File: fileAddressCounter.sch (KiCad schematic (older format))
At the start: 16 parts, among them U13 CD74AC161M, U14 CD74AC161M, U16 CD74AC161M, U17 CD74AC161M, U18 74AHC1G04, U19 CD74AC161M, U20 CD74AC161M, U38 74AHC1G04, U39 74AHC1G04

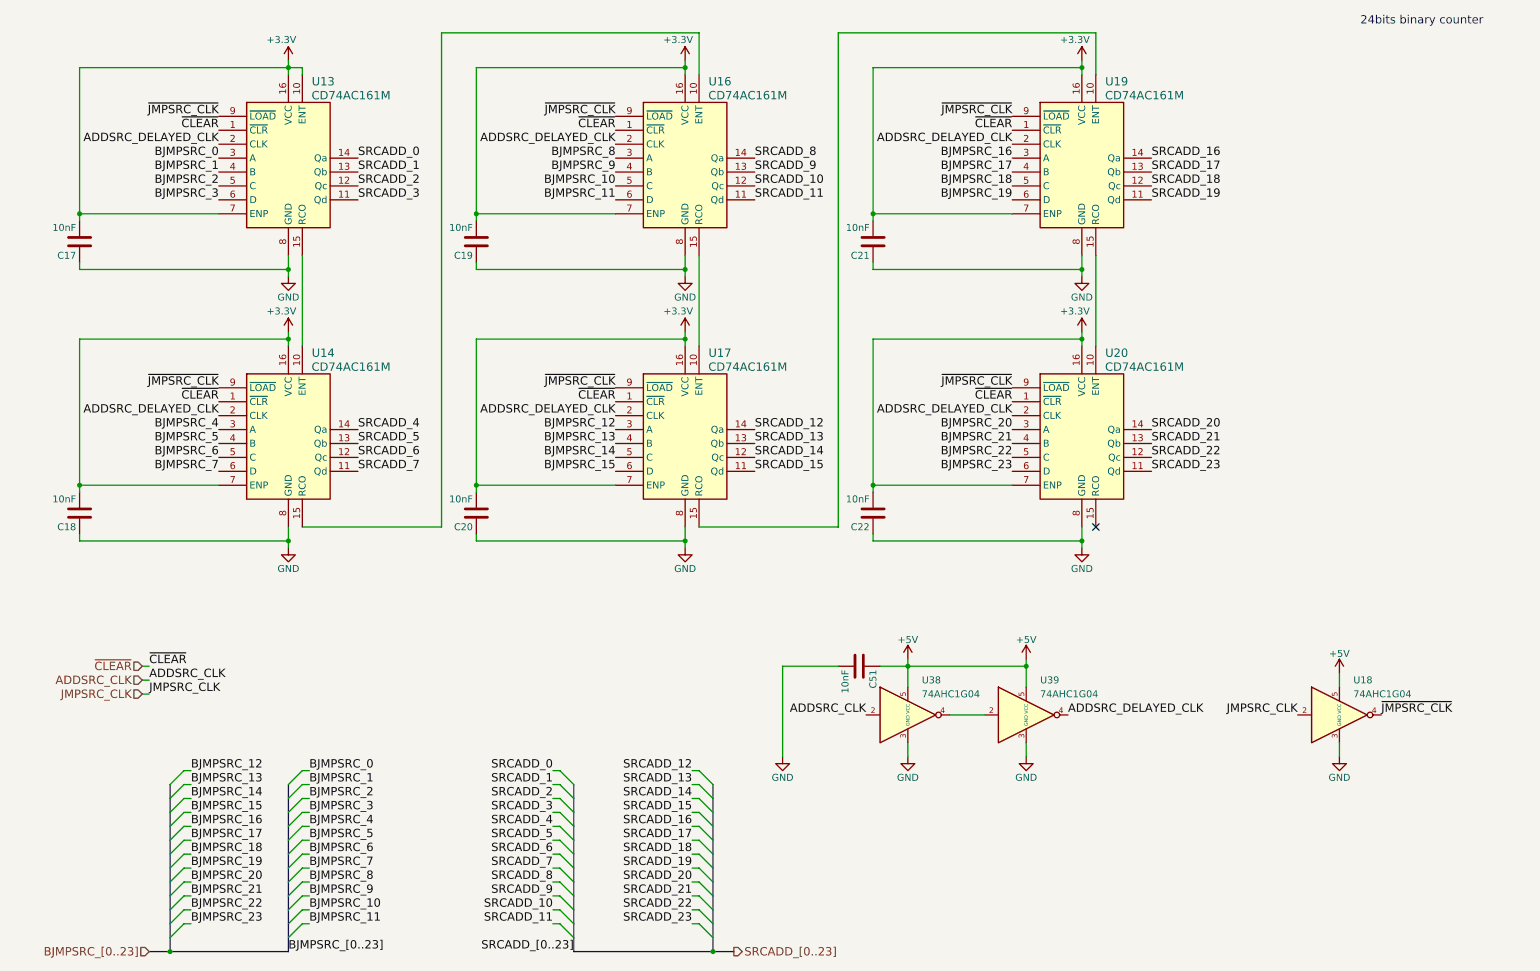
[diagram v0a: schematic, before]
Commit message: V5.1 (#15)
* Remove compatibility for 5.0, 4.x and add 5.1+

* Fix switched pins on SN74LV393A #7

* Removed capacitor on 12V #11

* Add/Modify power decoupling capacitor #10

* Removing ADDSCR_CLK delay #9

* Schematics : set version 5.1, 2021 copyright and publish date

* Put non-electrolytic capacitor #10

* Set every capacitor size to 0805

* Add new footprint for J7 TE_3-641124-6 #6

* Schematic : set pinHeader on J12 #4

* Netlist, apply change to board, clean track, #6 #4 #12 #10

* Set version to 5.1, 2021 copyright and date, replace the missing QRcode

* Back the MM1 connectors #8

* Replace capacitor for U22 U23 U24 #13

* Better decoupling

* Increase version, year to 2021, clear status

* Precise the molex connector for power supply

* First step, import ses

* Clean bottom layer

* #14 Set the BWRITE2 bus instead of BWRITE1 on U12

* netlist, redo autorouting and cleaning

* use shields.io for colored badge

* Update gerbert files

* Changelog, updated BOM

* Small revision on blockDiagram

* Update README.md

* exporting pcb in pdf

* 3D images, diagram.png

* Update schematics pdf

* redo wavedrom_24bitsCounter
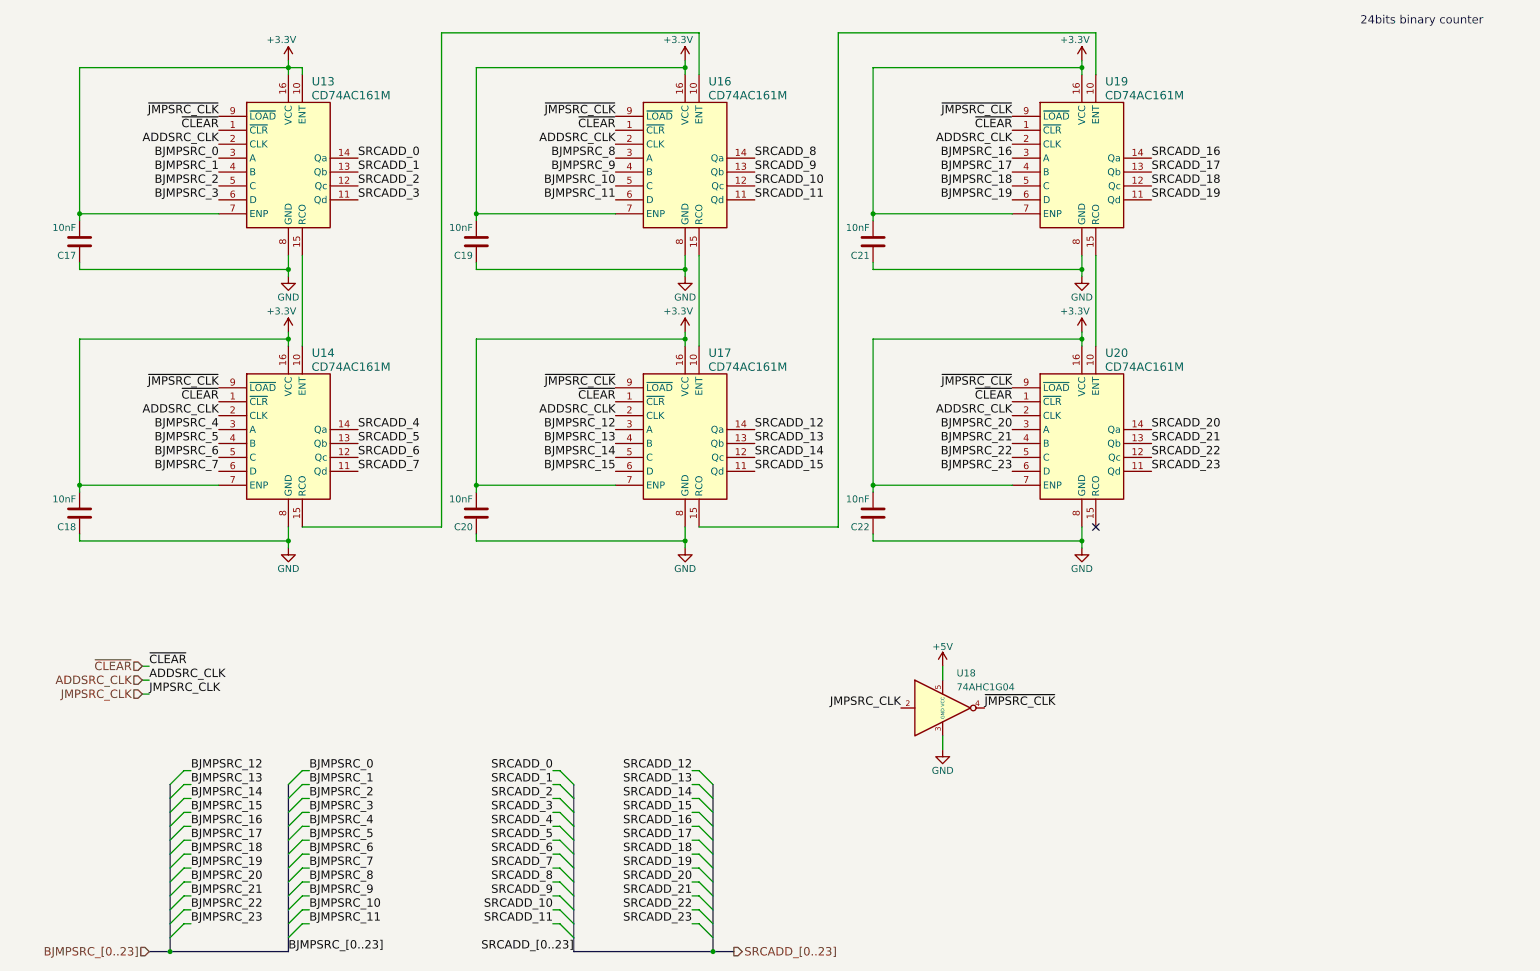
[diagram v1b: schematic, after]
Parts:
- removed C51: 10nF, Capacitor_SMD:C_0805_2012Metric, symbol Device:C
- removed U38, U39: 74AHC1G04, Package_TO_SOT_SMD:SOT-23-5, symbol Custom:74AHC1G04
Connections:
- net ADDSRC_DELAYED_CLK is gone; now on net ADDSRC_CLK: U13.2 (CLK), U14.2 (CLK), U16.2 (CLK), U17.2 (CLK), U19.2 (CLK), U20.2 (CLK)
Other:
- moved on the sheet: U18
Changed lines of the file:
@@
 Sheet 6 10
 Title "GCM"
-Date "2020-11-23"
-Rev "V5.0"
+Date "2021-02-16"
+Rev "V5.1"
 Comp "Guillaume Guillet"
-Comment1 "Copyright Guillaume Guillet 2020"
+Comment1 "Copyright Guillaume Guillet 2021"
 Comment2 "Licensed under CERN-OHL-W v2 or later"
 Comment3 ""
@@
 L power:GND #PWR083
 U 1 1 5BB5F937
-P 9950 5900
+P 7100 5850
 AR Path="/5BB5F937" Ref="#PWR083"  Part="1"
 AR Path="/5A93FC93/5BB5F937" Ref="#PWR083"  Part="1"
-F 0 "#PWR083" H 9950 5650 50  0001 C CNN
-F 1 "GND" H 9950 5750 50  0000 C CNN
-F 2 "" H 9950 5900 50  0001 C CNN
-F 3 "" H 9950 5900 50  0001 C CNN
-	1    9950 5900
+F 0 "#PWR083" H 7100 5600 50  0001 C CNN
+F 1 "GND" H 7100 5700 50  0000 C CNN
+F 2 "" H 7100 5850 50  0001 C CNN
+F 3 "" H 7100 5850 50  0001 C CNN
+	1    7100 5850
 	1    0    0    -1
 $EndComp
@@
 L power:+5V #PWR084
 U 1 1 5BB5F9A2
-P 9950 5300
+P 7100 5250
 AR Path="/5BB5F9A2" Ref="#PWR084"  Part="1"
 AR Path="/5A93FC93/5BB5F9A2" Ref="#PWR084"  Part="1"
-F 0 "#PWR084" H 9950 5150 50  0001 C CNN
-F 1 "+5V" H 9950 5440 50  0000 C CNN
-F 2 "" H 9950 5300 50  0001 C CNN
-F 3 "" H 9950 5300 50  0001 C CNN
-	1    9950 5300
-	1    0    0    -1
-$EndComp
-Text Label 9650 5600 2    60   ~ 0
+F 0 "#PWR084" H 7100 5100 50  0001 C CNN
+F 1 "+5V" H 7100 5390 50  0000 C CNN
+F 2 "" H 7100 5250 50  0001 C CNN
+F 3 "" H 7100 5250 50  0001 C CNN
+	1    7100 5250
+	1    0    0    -1
+$EndComp
+Text Label 6800 5550 2    60   ~ 0
 JMPSRC_CLK
-Text Label 10250 5600 0    60   ~ 0
+Text Label 7400 5550 0    60   ~ 0
 ~JMPSRC_CLK
 Text Label 2550 6000 0    60   ~ 0
@@
 L Custom:74AHC1G04 U?
 U 1 1 5F9095CA
-P 9950 5600
+P 7100 5550
 AR Path="/5F9095CA" Ref="U?"  Part="1"
 AR Path="/5A93FC93/5F9095CA" Ref="U18"  Part="1"
-F 0 "U18" H 10050 5850 50  0000 L CNN
-F 1 "74AHC1G04" H 10050 5750 50  0000 L CNN
-F 2 "Package_TO_SOT_SMD:SOT-23-5" H 9950 5600 50  0001 C CNN
-F 3 "https://assets.nexperia.com/documents/data-sheet/74AHC_AHCT1G04.pdf" H 9950 5600 50  0001 C CNN
-	1    9950 5600
-	1    0    0    -1
-$EndComp
-Wire Wire Line
-	9950 5900 9950 5800
-Wire Wire Line
-	9950 5400 9950 5300
-$Comp
-L power:GND #PWR?
-U 1 1 5FB1C83D
-P 7700 5900
-AR Path="/5FB1C83D" Ref="#PWR?"  Part="1"
-AR Path="/5A93FC93/5FB1C83D" Ref="#PWR0163"  Part="1"
-F 0 "#PWR0163" H 7700 5650 50  0001 C CNN
-F 1 "GND" H 7700 5750 50  0000 C CNN
-F 2 "" H 7700 5900 50  0001 C CNN
-F 3 "" H 7700 5900 50  0001 C CNN
-	1    7700 5900
-	1    0    0    -1
-$EndComp
-$Comp
-L power:+5V #PWR?
-U 1 1 5FB1C843
-P 7700 5200
-AR Path="/5FB1C843" Ref="#PWR?"  Part="1"
-AR Path="/5A93FC93/5FB1C843" Ref="#PWR0164"  Part="1"
-F 0 "#PWR0164" H 7700 5050 50  0001 C CNN
-F 1 "+5V" H 7700 5340 50  0000 C CNN
-F 2 "" H 7700 5200 50  0001 C CNN
-F 3 "" H 7700 5200 50  0001 C CNN
-	1    7700 5200
-	1    0    0    -1
-$EndComp
-$Comp
-L Custom:74AHC1G04 U?
-U 1 1 5FB1C84B
-P 7700 5600
-AR Path="/5FB1C84B" Ref="U?"  Part="1"
-AR Path="/5A93FC93/5FB1C84B" Ref="U39"  Part="1"
-F 0 "U39" H 7800 5850 50  0000 L CNN
-F 1 "74AHC1G04" H 7800 5750 50  0000 L CNN
-F 2 "Package_TO_SOT_SMD:SOT-23-5" H 7700 5600 50  0001 C CNN
-F 3 "https://assets.nexperia.com/documents/data-sheet/74AHC_AHCT1G04.pdf" H 7700 5600 50  0001 C CNN
-	1    7700 5600
-	1    0    0    -1
-$EndComp
-Wire Wire Line
-	7700 5900 7700 5800
-$Comp
-L power:GND #PWR?
-U 1 1 5FB2A8C2
-P 6850 5900
-AR Path="/5FB2A8C2" Ref="#PWR?"  Part="1"
-AR Path="/5A93FC93/5FB2A8C2" Ref="#PWR0165"  Part="1"
-F 0 "#PWR0165" H 6850 5650 50  0001 C CNN
-F 1 "GND" H 6850 5750 50  0000 C CNN
-F 2 "" H 6850 5900 50  0001 C CNN
-F 3 "" H 6850 5900 50  0001 C CNN
-	1    6850 5900
-	1    0    0    -1
-$EndComp
-$Comp
-L power:+5V #PWR?
-U 1 1 5FB2A8C8
-P 6850 5200
-AR Path="/5FB2A8C8" Ref="#PWR?"  Part="1"
-AR Path="/5A93FC93/5FB2A8C8" Ref="#PWR0166"  Part="1"
-F 0 "#PWR0166" H 6850 5050 50  0001 C CNN
-F 1 "+5V" H 6850 5340 50  0000 C CNN
-F 2 "" H 6850 5200 50  0001 C CNN
-F 3 "" H 6850 5200 50  0001 C CNN
-	1    6850 5200
-	1    0    0    -1
-$EndComp
-$Comp
-L Custom:74AHC1G04 U?
-U 1 1 5FB2A8CE
-P 6850 5600
-AR Path="/5FB2A8CE" Ref="U?"  Part="1"
-AR Path="/5A93FC93/5FB2A8CE" Ref="U38"  Part="1"
-F 0 "U38" H 6950 5850 50  0000 L CNN
-F 1 "74AHC1G04" H 6950 5750 50  0000 L CNN
-F 2 "Package_TO_SOT_SMD:SOT-23-5" H 6850 5600 50  0001 C CNN
-F 3 "https://assets.nexperia.com/documents/data-sheet/74AHC_AHCT1G04.pdf" H 6850 5600 50  0001 C CNN
-	1    6850 5600
-	1    0    0    -1
-$EndComp
-Wire Wire Line
-	6850 5900 6850 5800
-Text Label 6550 5600 2    60   ~ 0
+F 0 "U18" H 7200 5800 50  0000 L CNN
+F 1 "74AHC1G04" H 7200 5700 50  0000 L CNN
+F 2 "Package_TO_SOT_SMD:SOT-23-5" H 7100 5550 50  0001 C CNN
+F 3 "https://assets.nexperia.com/documents/data-sheet/74AHC_AHCT1G04.pdf" H 7100 5550 50  0001 C CNN
+	1    7100 5550
+	1    0    0    -1
+$EndComp
+Wire Wire Line
+	7100 5850 7100 5750
+Wire Wire Line
+	7100 5350 7100 5250
+Text Label 7600 3450 2    60   ~ 0
 ADDSRC_CLK
-Text Label 8000 5600 0    60   ~ 0
-ADDSRC_DELAYED_CLK
-$Comp
-L Device:C C?
-U 1 1 5FB4378B
-P 6500 5250
-AR Path="/5FB4378B" Ref="C?"  Part="1"
-AR Path="/5A93FC93/5FB4378B" Ref="C51"  Part="1"
-F 0 "C51" H 6525 5350 50  0000 L CNN
-F 1 "10nF" H 6525 5150 50  0000 L CNN
-F 2 "Capacitor_SMD:C_0805_2012Metric" H 6538 5100 50  0001 C CNN
-F 3 "" H 6500 5250 50  0001 C CNN
-	1    6500 5250
-	0    1    1    0
-$EndComp
-Wire Wire Line
-	7700 5200 7700 5250
-Wire Wire Line
-	7700 5250 6850 5250
-Wire Wire Line
-	6850 5250 6850 5200
-Connection ~ 7700 5250
-Wire Wire Line
-	7700 5250 7700 5400
-Wire Wire Line
-	6850 5250 6850 5400
-Connection ~ 6850 5250
-Wire Wire Line
-	6850 5250 6650 5250
-Wire Wire Line
-	6350 5250 5950 5250
-Wire Wire Line
-	5950 5250 5950 5900
-$Comp
-L power:GND #PWR?
-U 1 1 5FB666FB
-P 5950 5900
-AR Path="/5FB666FB" Ref="#PWR?"  Part="1"
-AR Path="/5A93FC93/5FB666FB" Ref="#PWR0167"  Part="1"
-F 0 "#PWR0167" H 5950 5650 50  0001 C CNN
-F 1 "GND" H 5950 5750 50  0000 C CNN
-F 2 "" H 5950 5900 50  0001 C CNN
-F 3 "" H 5950 5900 50  0001 C CNN
-	1    5950 5900
-	1    0    0    -1
-$EndComp
-Wire Wire Line
-	7400 5600 7150 5600
 $Comp
 L Custom:CD74AC161M U19
@@
 	1    0    0    -1
 $EndComp
-Text Label 7600 1500 2    60   ~ 0
-ADDSRC_DELAYED_CLK
 Wire Wire Line
 	7600 2000 6600 2000
@@
 	1    0    0    -1
 $EndComp
-Text Label 7600 3450 2    60   ~ 0
-ADDSRC_DELAYED_CLK
 Wire Wire Line
 	7600 3950 6600 3950
@@
 	1    0    0    -1
 $EndComp
-Text Label 4750 1500 2    60   ~ 0
-ADDSRC_DELAYED_CLK
 Wire Wire Line
 	4750 2000 3750 2000
@@
 	3750 4000 3750 3950
 Connection ~ 3750 3950
-Text Label 4750 3450 2    60   ~ 0
-ADDSRC_DELAYED_CLK
 $Comp
 L Device:C C?
@@
 	1    0    0    -1
 $EndComp
-Text Label 1900 1500 2    60   ~ 0
-ADDSRC_DELAYED_CLK
 Wire Wire Line
 	1900 2000 900  2000
@@
 	900  4000 900  3950
 Connection ~ 900  3950
-Text Label 1900 3450 2    60   ~ 0
-ADDSRC_DELAYED_CLK
 Wire Wire Line
 	2500 1000 2500 950
@@
 	1    0    0    -1
 $EndComp
+Text Label 7600 1500 2    60   ~ 0
+ADDSRC_CLK
+Text Label 4750 1500 2    60   ~ 0
+ADDSRC_CLK
+Text Label 1900 1500 2    60   ~ 0
+ADDSRC_CLK
+Text Label 1900 3450 2    60   ~ 0
+ADDSRC_CLK
+Text Label 4750 3450 2    60   ~ 0
+ADDSRC_CLK
 Wire Bus Line
 	5450 6100 5450 7300
